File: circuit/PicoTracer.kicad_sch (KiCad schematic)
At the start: 36 parts, among them J1 Conn_01x04_Socket, J2 Conn_01x04_Socket, J3 Conn_01x08_Socket, J6 Conn_01x04_Socket, J7 8P8C, SW1 SW_Push, SW2 SW_Push, U1 Pico, U2 MCP3002, U3 MCP3002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

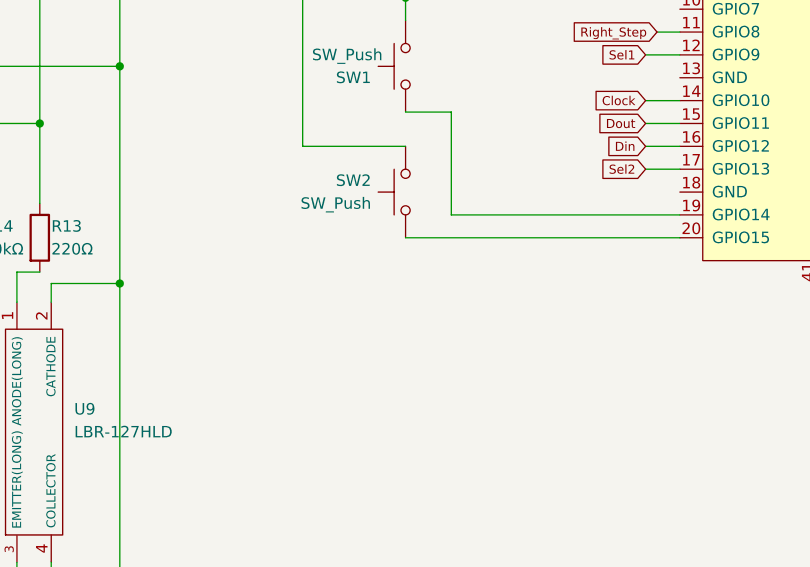
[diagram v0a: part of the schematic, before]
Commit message: pullup用抵抗を追加（未試験のため検証して動きに問題なければつなぐ）
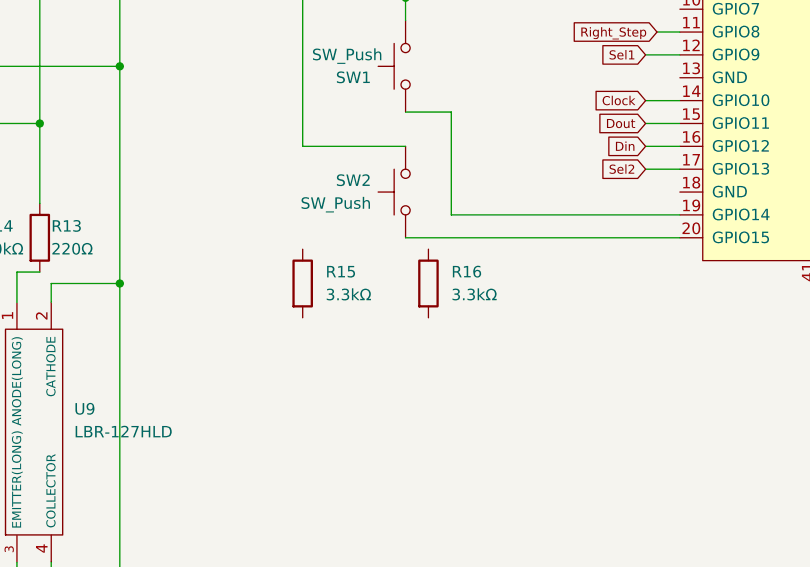
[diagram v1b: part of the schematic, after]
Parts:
- added R15, R16: 3.3kΩ, symbol Device:R
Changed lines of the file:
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@@
+    )
+  )
+  (symbol (lib_id "Device:R") (at 167.64 161.29 0) (unit 1)
+    (in_bom yes) (on_board yes) (dnp no) (fields_autoplaced)
+    (property "Reference" "R15" (at 170.18 160.02 0)
+      (effects (font (size 1.27 1.27)) (justify left))
+    )
+    (property "Value" "3.3kΩ" (at 170.18 162.56 0)
+      (effects (font (size 1.27 1.27)) (justify left))
+    )
+    (property "Footprint" "" (at 165.862 161.29 90)
+      (effects (font (size 1.27 1.27)) hide)
+    )
+    (property "Datasheet" "~" (at 167.64 161.29 0)
+      (effects (font (size 1.27 1.27)) hide)
+    )
+    (pin "2")
+    (pin "1")
+    (instances
+      (project "PicoTracer"
+        (path "/f79d951e-a1b3-4edf-883f-79f37eda87da"
+          (reference "R15") (unit 1)
+        )
+      )
     )
   )
@@
         )
       )
+    )
+  )
+  (symbol (lib_id "Device:R") (at 181.61 161.29 0) (unit 1)
+    (in_bom yes) (on_board yes) (dnp no) (fields_autoplaced)
+    (property "Reference" "R16" (at 184.15 160.02 0)
+      (effects (font (size 1.27 1.27)) (justify left))
+    )
+    (property "Value" "3.3kΩ" (at 184.15 162.56 0)
+      (effects (font (size 1.27 1.27)) (justify left))
+    )
+    (property "Footprint" "" (at 179.832 161.29 90)
+      (effects (font (size 1.27 1.27)) hide)
+    )
+    (property "Datasheet" "~" (at 181.61 161.29 0)
+      (effects (font (size 1.27 1.27)) hide)
+    )
+    (pin "2")
+    (pin "1")
+    (instances
+      (project "PicoTracer"
+        (path "/f79d951e-a1b3-4edf-883f-79f37eda87da"
+          (reference "R16") (unit 1)
+        )
+      )

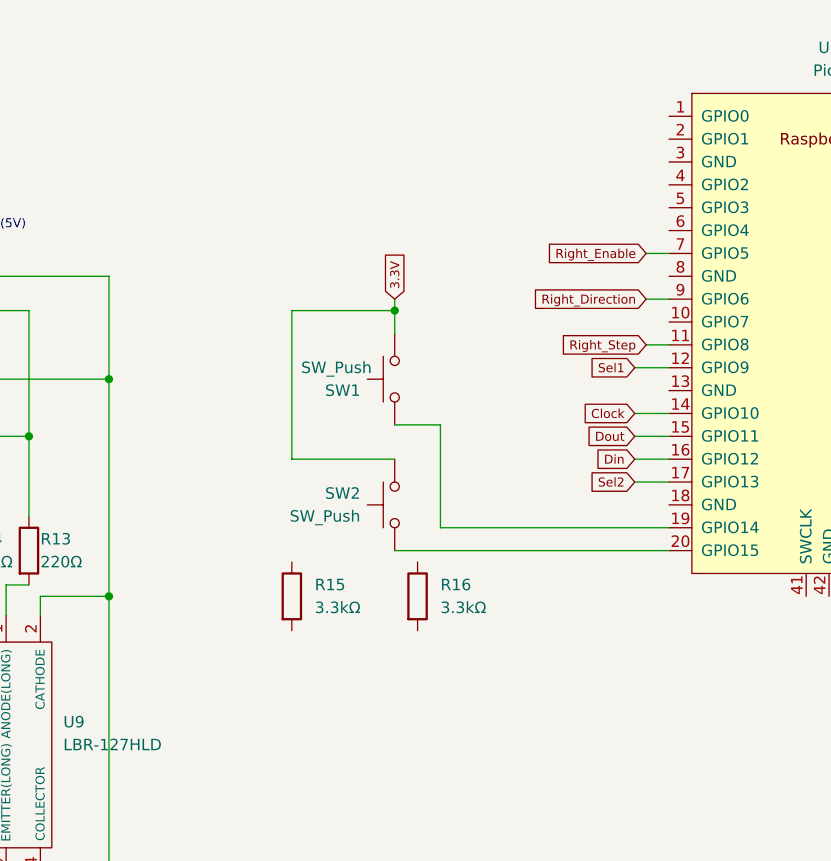
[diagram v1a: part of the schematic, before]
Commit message: プッシュスイッチにPullup抵抗を追加
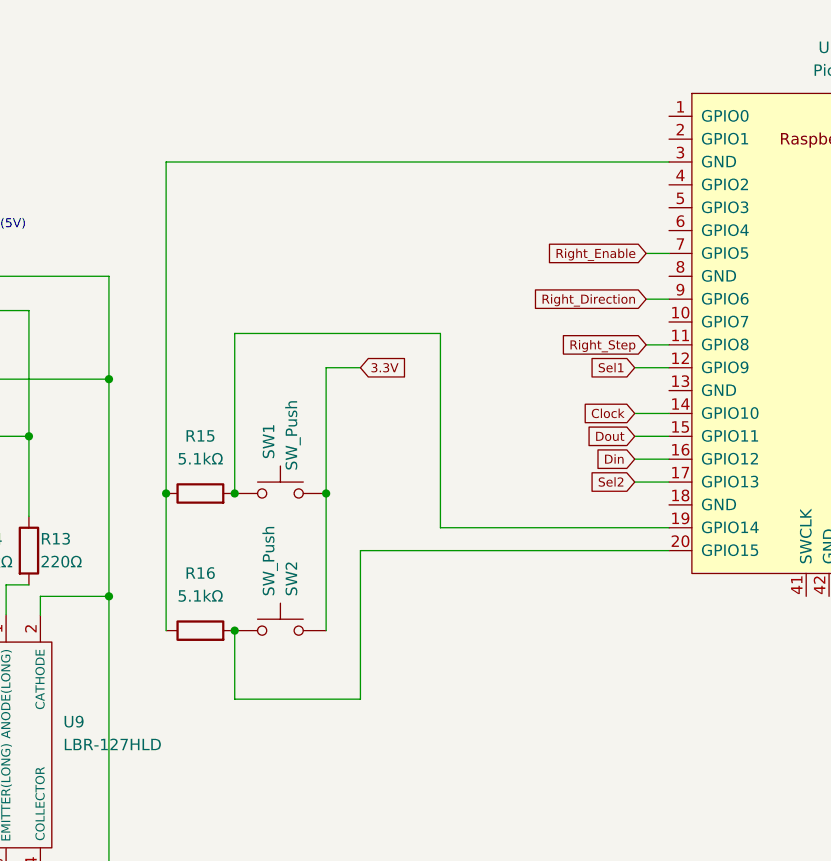
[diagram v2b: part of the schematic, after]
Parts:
- R15, R16: value 3.3kΩ -> 5.1kΩ
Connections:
- net at SW2.2, U1.20 (GPIO15): now also R16.2
- net at SW1.1, U1.19 (GPIO14): now also R15.2
- net at U1.3 (GND): now also R15.1, R16.1
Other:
- moved on the sheet: R16, SW1, SW2

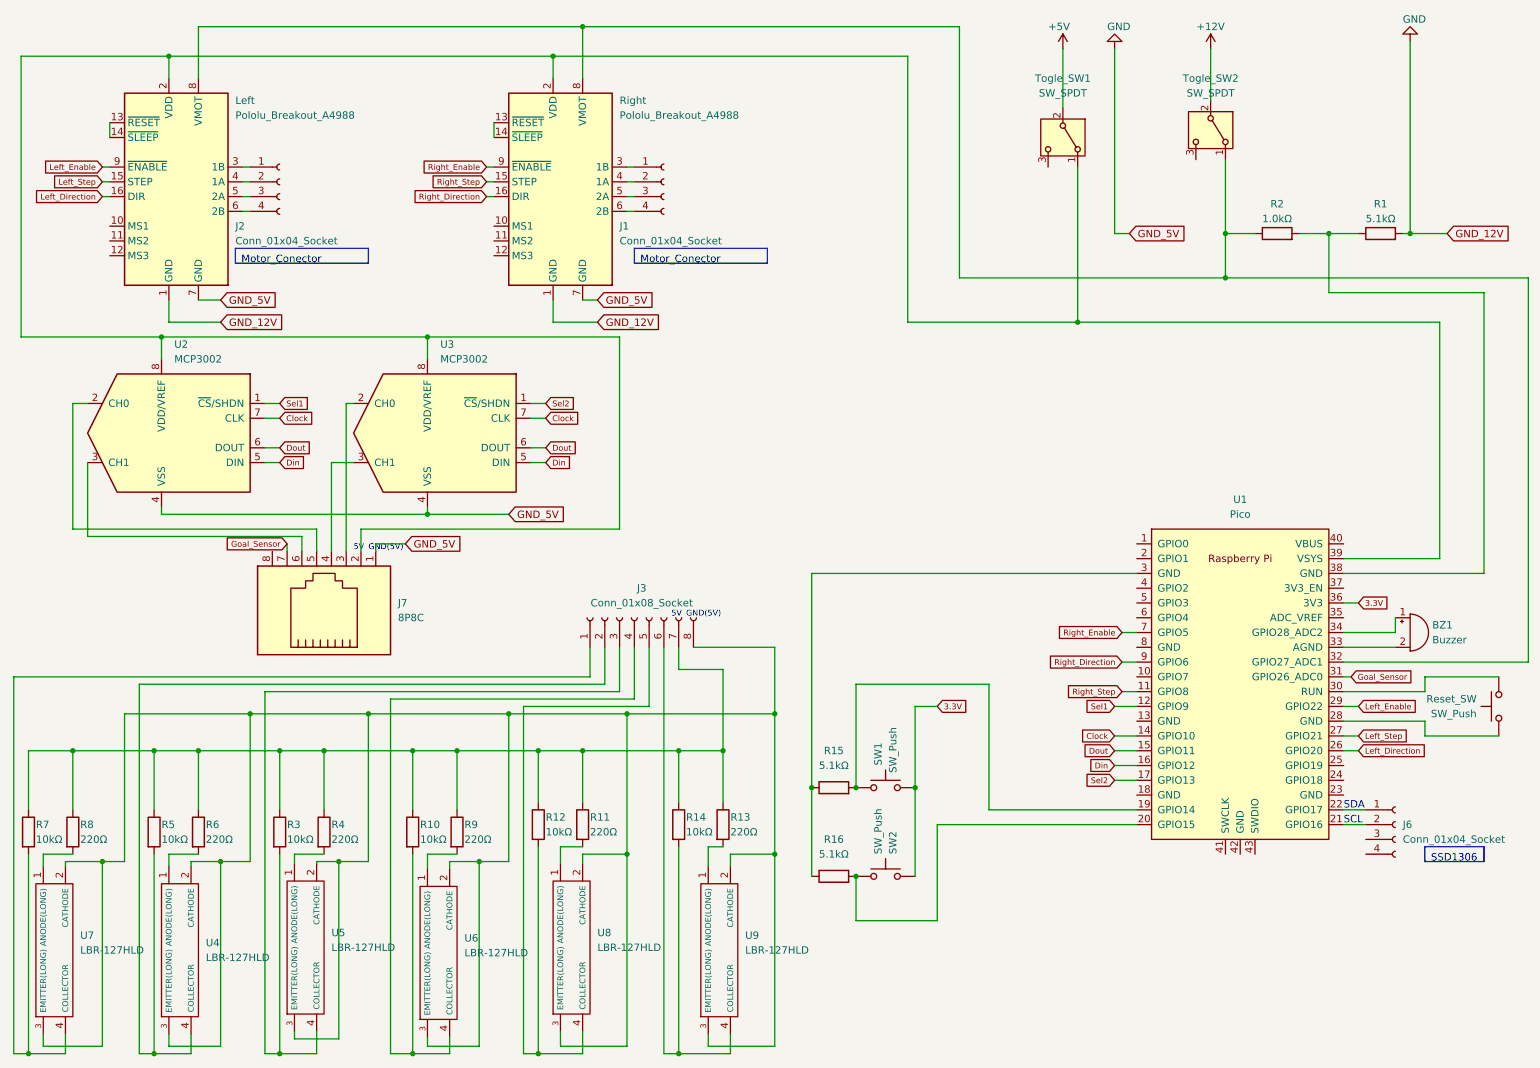
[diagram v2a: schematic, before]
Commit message: 回路図いったん完成、PCBファイルに基盤外形追加
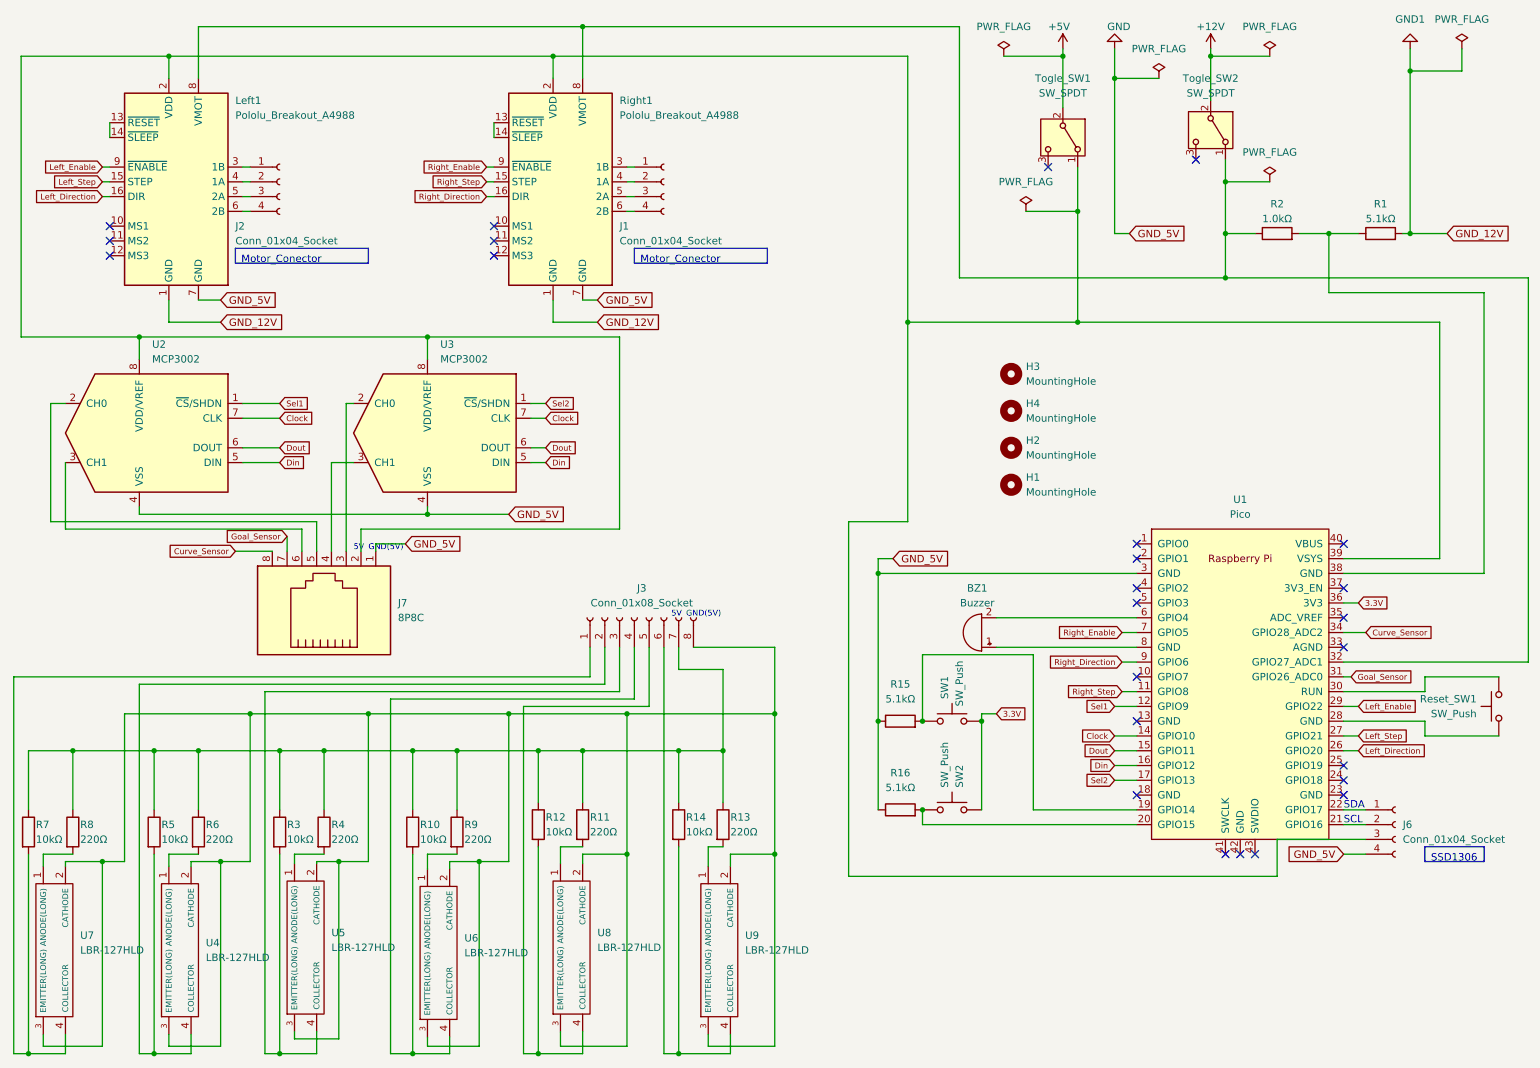
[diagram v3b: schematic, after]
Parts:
- added H1, H2, H3, H4: MountingHole, symbol Mechanical:MountingHole
- renumbered Left to Left1, Reset_SW to Reset_SW1, Right to Right1
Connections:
- net GND: now also J6.4 (Pin_4), R15.1, R16.1, U1.3 (GND); no longer Left1.1 (GND), R1.2, Right1.1 (GND)
- net at J6.3 (Pin_3): now also J7.2, Left1.2 (VDD), Right1.2 (VDD), Togle_SW1.1 (A), U1.39 (VSYS), U2.8 (VDD/VREF), U3.8 (VDD/VREF)
- net Curve_Sensor: now reaches J7.8
- net Curve_Sensor: now also U1.34 (GPIO28_ADC2)
- net at U1.33 (AGND): no longer BZ1.2 (-)
- net at BZ1.1 (+): now also U1.8 (GND); no longer U1.34 (GPIO28_ADC2)
- net at U1.6 (GPIO4): now also BZ1.2 (-)
- new net GND1: Left1.1 (GND), R1.2, Right1.1 (GND)
- no-connect marks 0 -> 25
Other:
- moved on the sheet: BZ1, R15, R16, SW1, SW2, U2

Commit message: 回路図：完成、配線図：配置のみ完了
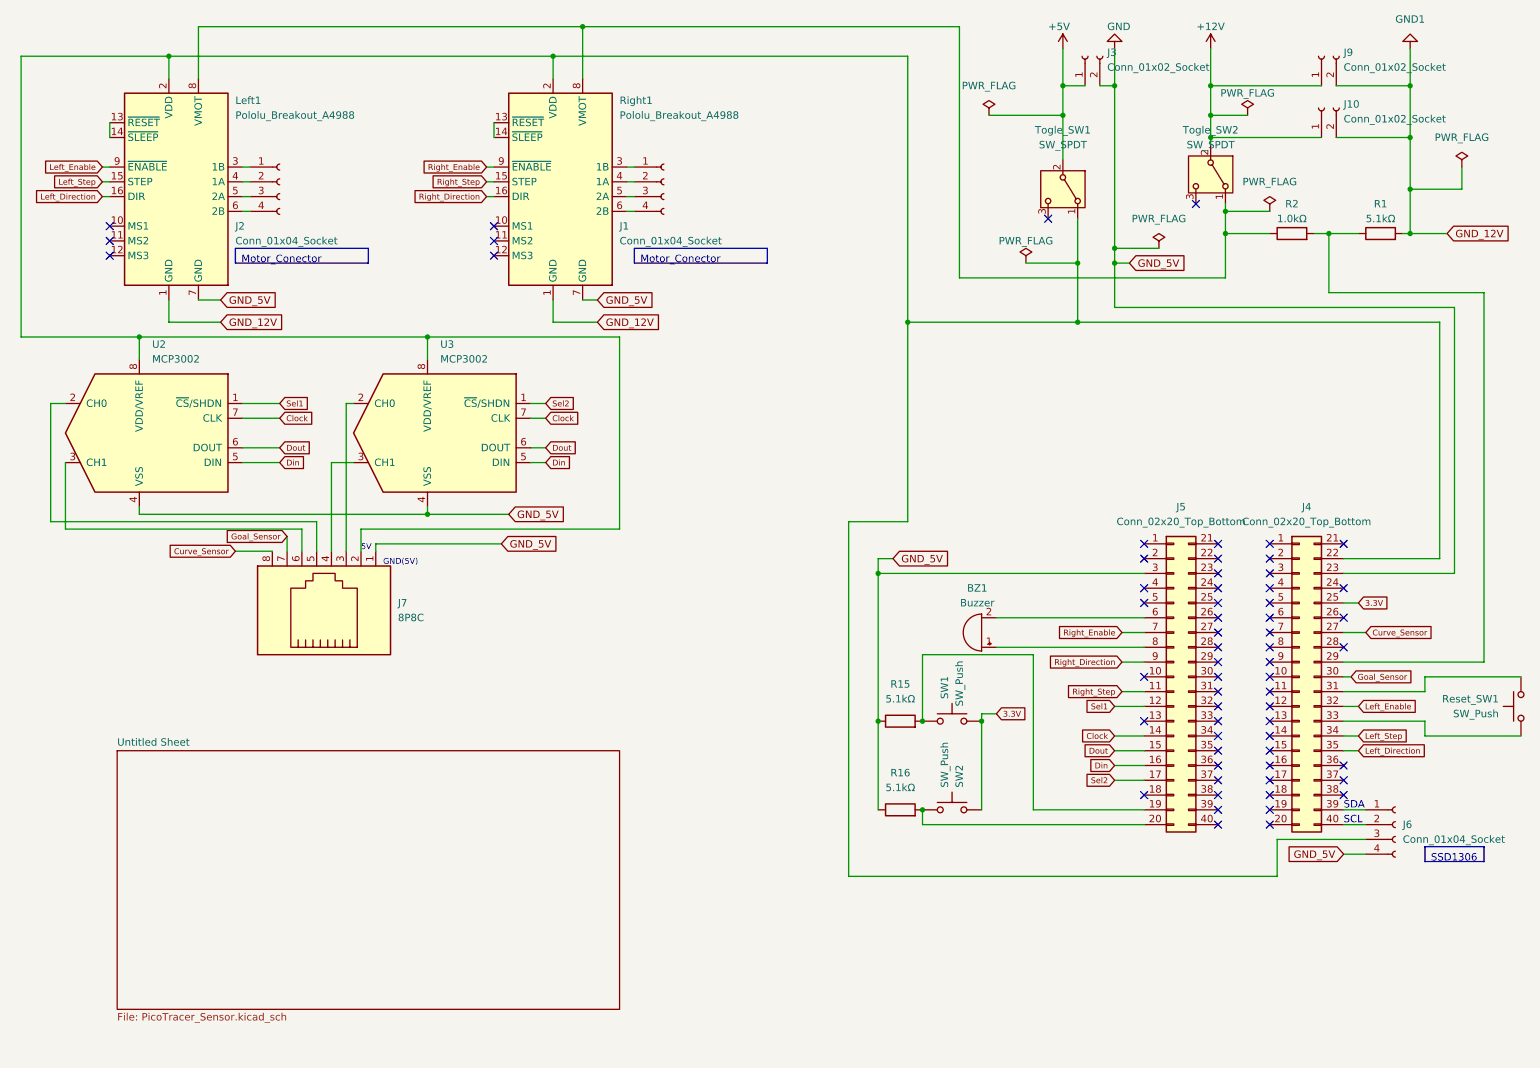
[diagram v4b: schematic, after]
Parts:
- removed H1, H2, H3, H4: MountingHole, symbol Mechanical:MountingHole
- removed J3: Conn_01x08_Socket, symbol Connector:Conn_01x08_Socket
- removed R10, R12, R14, R3, R5, R7: 10kΩ, symbol Device:R
- removed R11, R13, R4, R6, R8, R9: 220Ω, symbol Device:R
- removed U1: Pico, RPi_Pico:RPi_Pico_SMD_TH, symbol RPi_Pico:Pico
- removed U4, U5, U6, U7, U8, U9: LBR-127HLD, LBR127HLD, symbol SamacSys_Parts:LBR-127HLD
- added J10, J9: Conn_01x02_Socket, Connector_JST:JST_VH_B2P-VH_1x02_P3.96mm_Vertical, symbol Connector:Conn_01x02_Socket
- added J3: Conn_01x02_Socket, Connector_JST:JST_XH_B2B-XH-A_1x02_P2.50mm_Vertical, symbol Connector:Conn_01x02_Socket
- added J4, J5: Conn_02x20_Top_Bottom, Connector_PinSocket_2.54mm:PinSocket_2x20_P2.54mm_Vertical_Raspipico, symbol Connector_Generic:Conn_02x20_Top_Bottom
- BZ1: footprint (none) -> Buzzer_Beeper:Buzzer_15x7.5RM7.6
- J1, J2: footprint (none) -> Connector_JST:JST_XH_S4B-XH-A_1x04_P2.50mm_Horizontal
- J6: footprint (none) -> Connector_PinHeader_2.54mm:PinHeader_1x04_P2.54mm_Vertical
- J7: footprint (none) -> Connector_PinHeader_2.54mm:PinHeader_1x08_P2.54mm_Vertical
- R1, R15, R16, R2: footprint (none) -> Resistor_THT:R_Axial_DIN0207_L6.3mm_D2.5mm_P7.62mm_Horizontal
- Reset_SW1, SW1, SW2: footprint (none) -> Button_Switch_THT:SW_PUSH_6mm_H4.3mm
- Togle_SW1, Togle_SW2: footprint (none) -> SamacSys_Parts:2MS1T1B4VS2QES
- U2, U3: footprint (none) -> SamacSys_Parts:DIP781W56P254L950H533Q8N
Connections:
- net +12V: now also J10.1 (Pin_1), J9.1 (Pin_1)
- net +5V: now also J3.1 (Pin_1)
- net 3.3V: now also J4.25 (Pin_25)
- net Clock: now also J5.14 (Pin_14)
- net Curve_Sensor: now also J4.27 (Pin_27)
- net Din: now also J5.16 (Pin_16)
- net Dout: now also J5.15 (Pin_15)
- net GND: now also J3.2 (Pin_2), J4.23 (Pin_23), J5.3 (Pin_3)
- net GND1: now also J10.2 (Pin_2), J9.2 (Pin_2)
- net Goal_Sensor: now also J4.30 (Pin_30)
- net Left_Direction: now also J4.35 (Pin_35)
- net Left_Enable: now also J4.32 (Pin_32)
- net Left_Step: now also J4.34 (Pin_34)
- net Right_Direction: now also J5.9 (Pin_9)
- net Right_Enable: now also J5.7 (Pin_7)
- net Right_Step: now also J5.11 (Pin_11)
- net Sel1: now also J5.12 (Pin_12)
- net Sel2: now also J5.17 (Pin_17)
- net at R15.2, SW1.1: now also J5.19 (Pin_19)
- net at J6.1 (Pin_1): now also J4.39 (Pin_39)
- net at J6.2 (Pin_2): now also J4.40 (Pin_40)
- net at J6.3 (Pin_3), J7.2, Left1.2 (VDD)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: now also J4.22 (Pin_22)
- net at R16.2, SW2.2: now also J5.20 (Pin_20)
- net at R1.1, R2.2: now also J4.29 (Pin_29)
- net at Reset_SW1.2: now also J4.33 (Pin_33)
- net at Reset_SW1.1: now also J4.31 (Pin_31)
- net at BZ1.2 (-): now also J5.6 (Pin_6)
- net at BZ1.1 (+): now also J5.8 (Pin_8)
- no-connect marks 25 -> 62
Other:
- added sheet Untitled Sheet (PicoTracer_Sensor.kicad_sch)
- moved on the sheet: R2, Reset_SW1, Togle_SW1, Togle_SW2
